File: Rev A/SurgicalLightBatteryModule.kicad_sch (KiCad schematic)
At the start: 0 parts

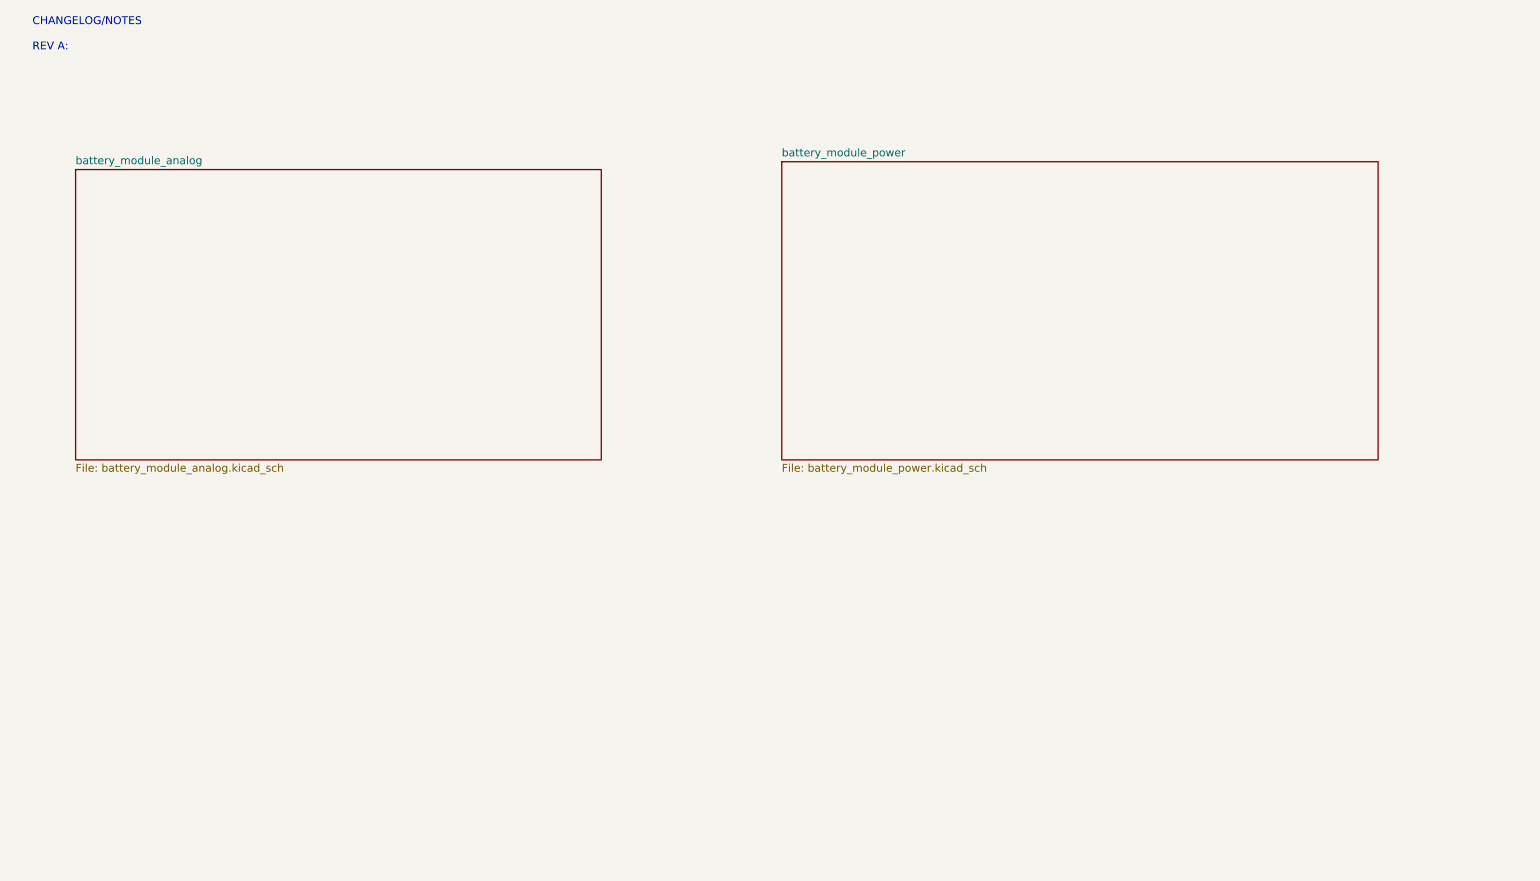
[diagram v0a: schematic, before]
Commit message: Added buck converter schematic.
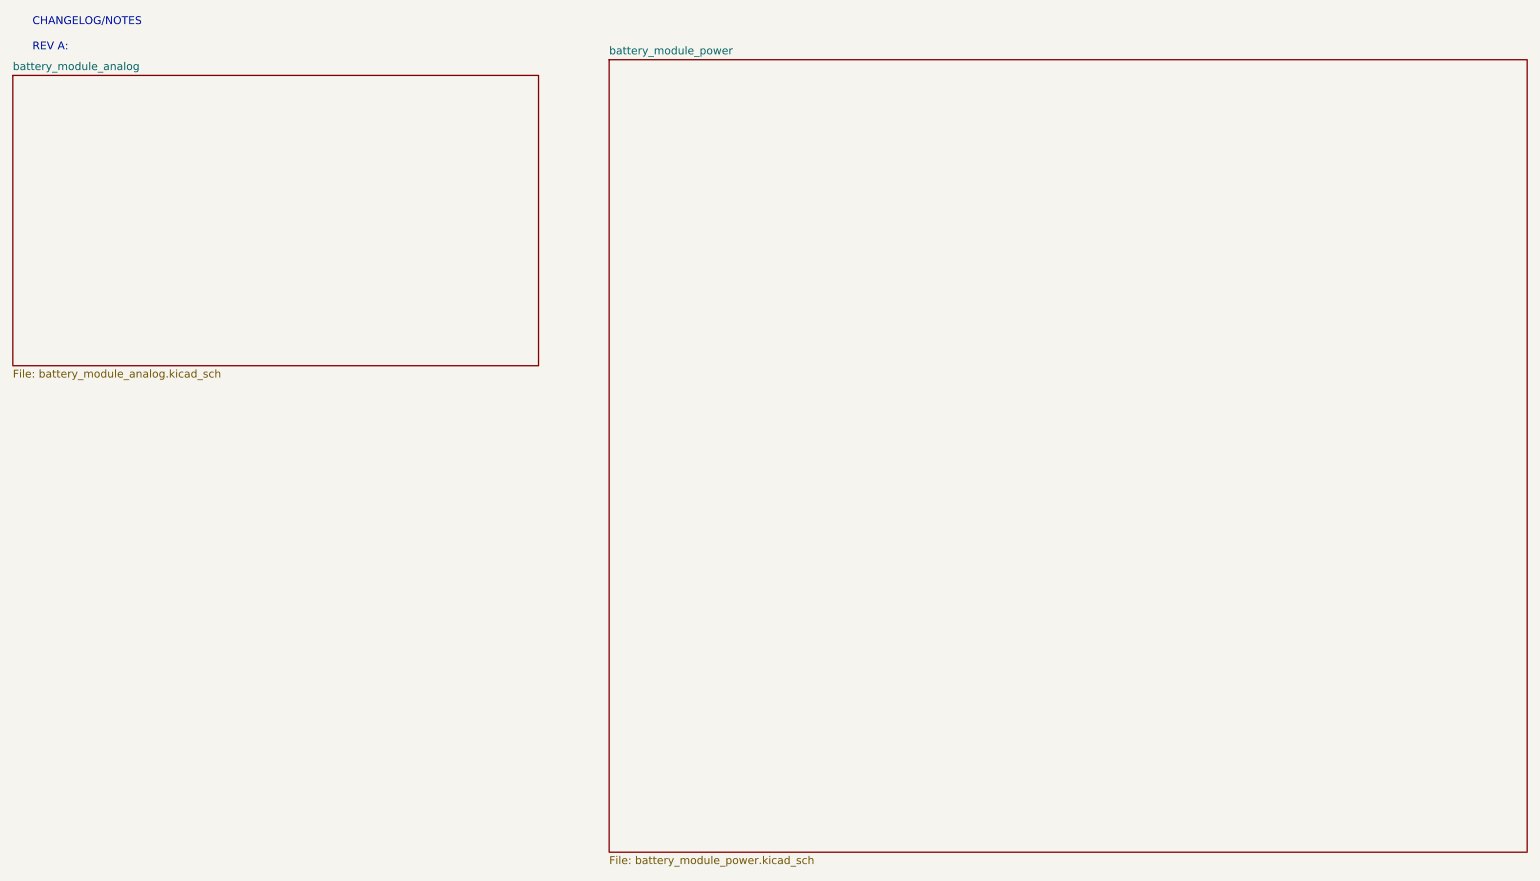
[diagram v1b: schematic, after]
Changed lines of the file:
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@@
 	)
 	(sheet
-		(at 140.97 40.64)
-		(size 96.52 48.26)
+		(at 113.03 24.13)
+		(size 148.59 128.27)
 		(fields_autoplaced yes)
 		(stroke
@@
 		)
 		(property "Sheetname" "battery_module_power"
-			(at 140.97 39.9284 0)
+			(at 113.03 23.4184 0)
 			(effects
 				(font
@@
 		)
 		(property "Sheetfile" "battery_module_power.kicad_sch"
-			(at 140.97 89.4846 0)
+			(at 113.03 152.9846 0)
 			(effects
 				(font
@@
 	)
 	(sheet
-		(at 26.67 41.91)
+		(at 16.51 26.67)
 		(size 85.09 46.99)
 		(fields_autoplaced yes)
@@
 		)
 		(property "Sheetname" "battery_module_analog"
-			(at 26.67 41.1984 0)
+			(at 16.51 25.9584 0)
 			(effects
 				(font
@@
 		)
 		(property "Sheetfile" "battery_module_analog.kicad_sch"
-			(at 26.67 89.4846 0)
+			(at 16.51 74.2446 0)
 			(effects
 				(font
